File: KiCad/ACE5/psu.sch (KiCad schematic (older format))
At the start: 29 parts, among them IC1 LM7805MPX_NOPB

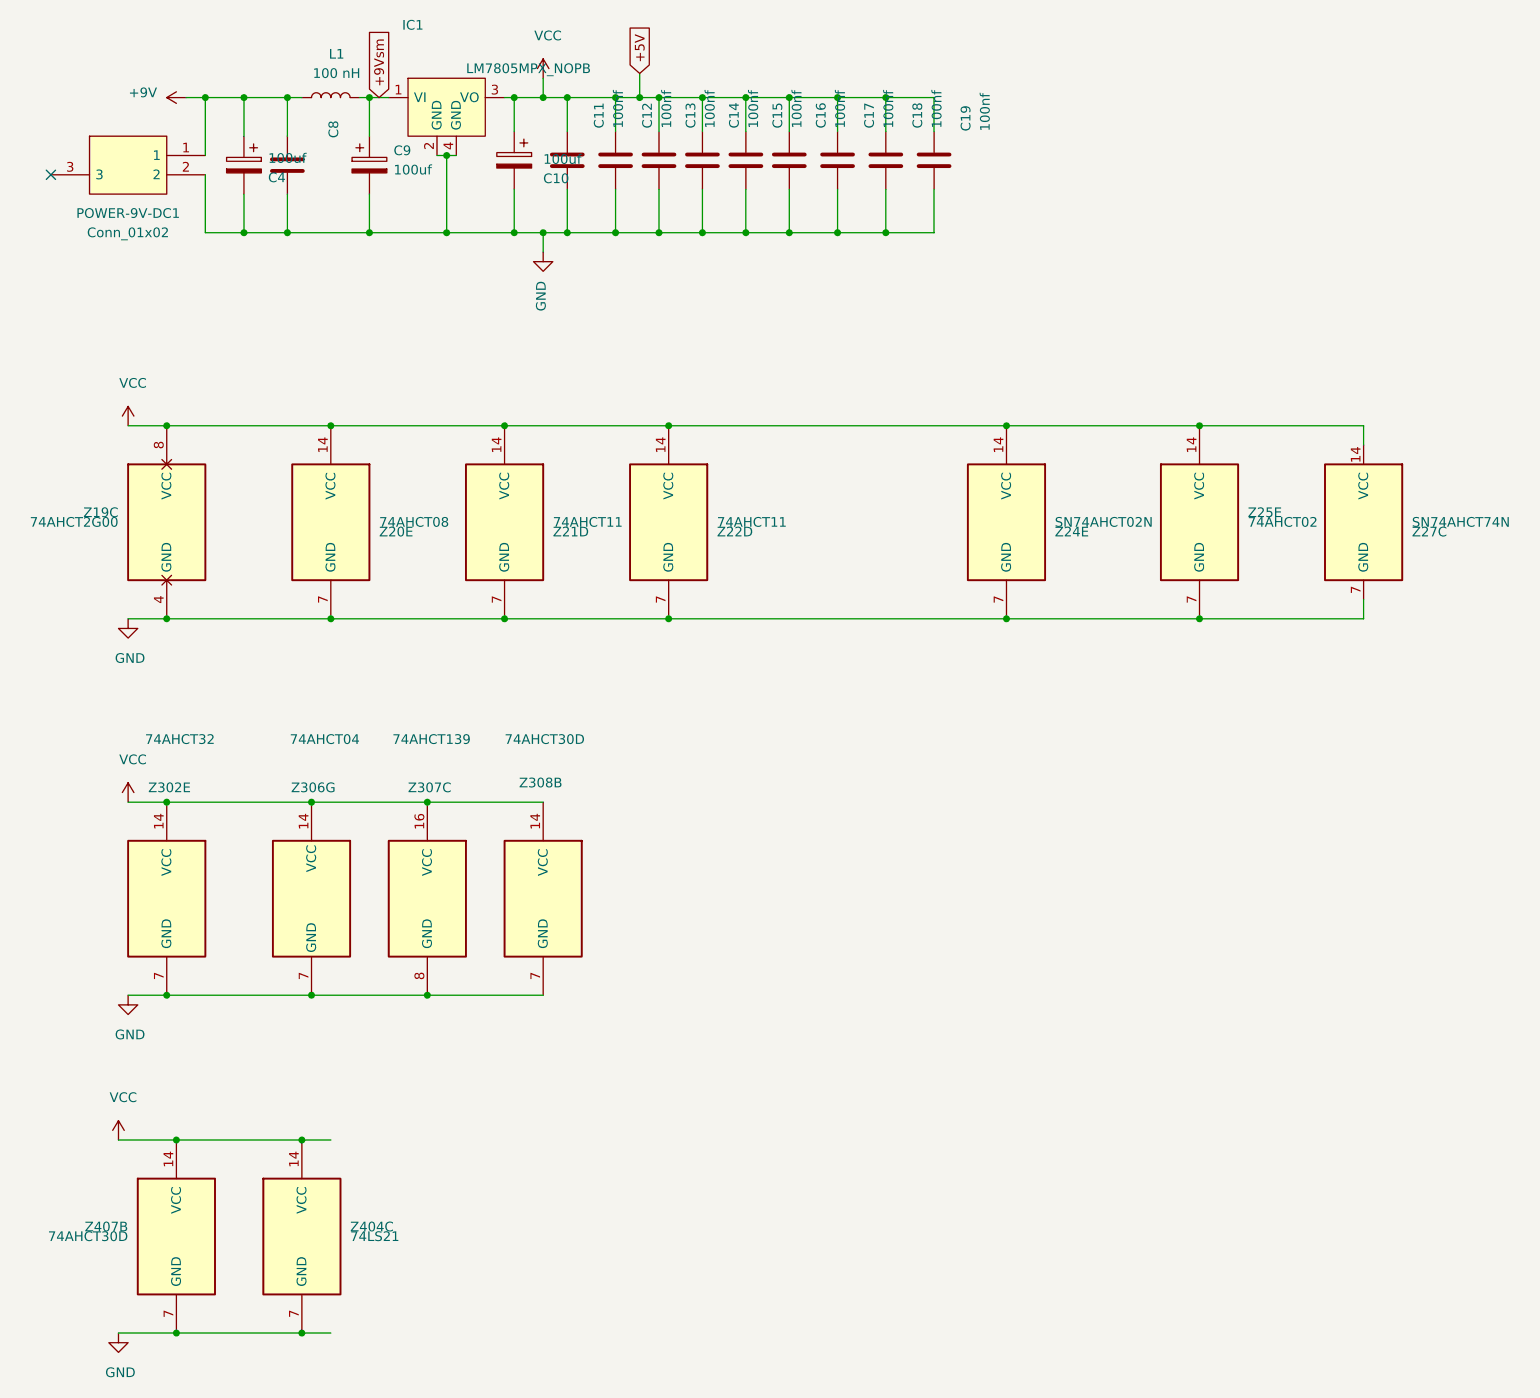
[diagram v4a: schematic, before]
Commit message: Fix several problems with Chip Select. Reconnect the Data bus for the VDG to the CPU bus which has become disconnected.
Signed-off-by: John Bradley <flypie@rocketmail.com>
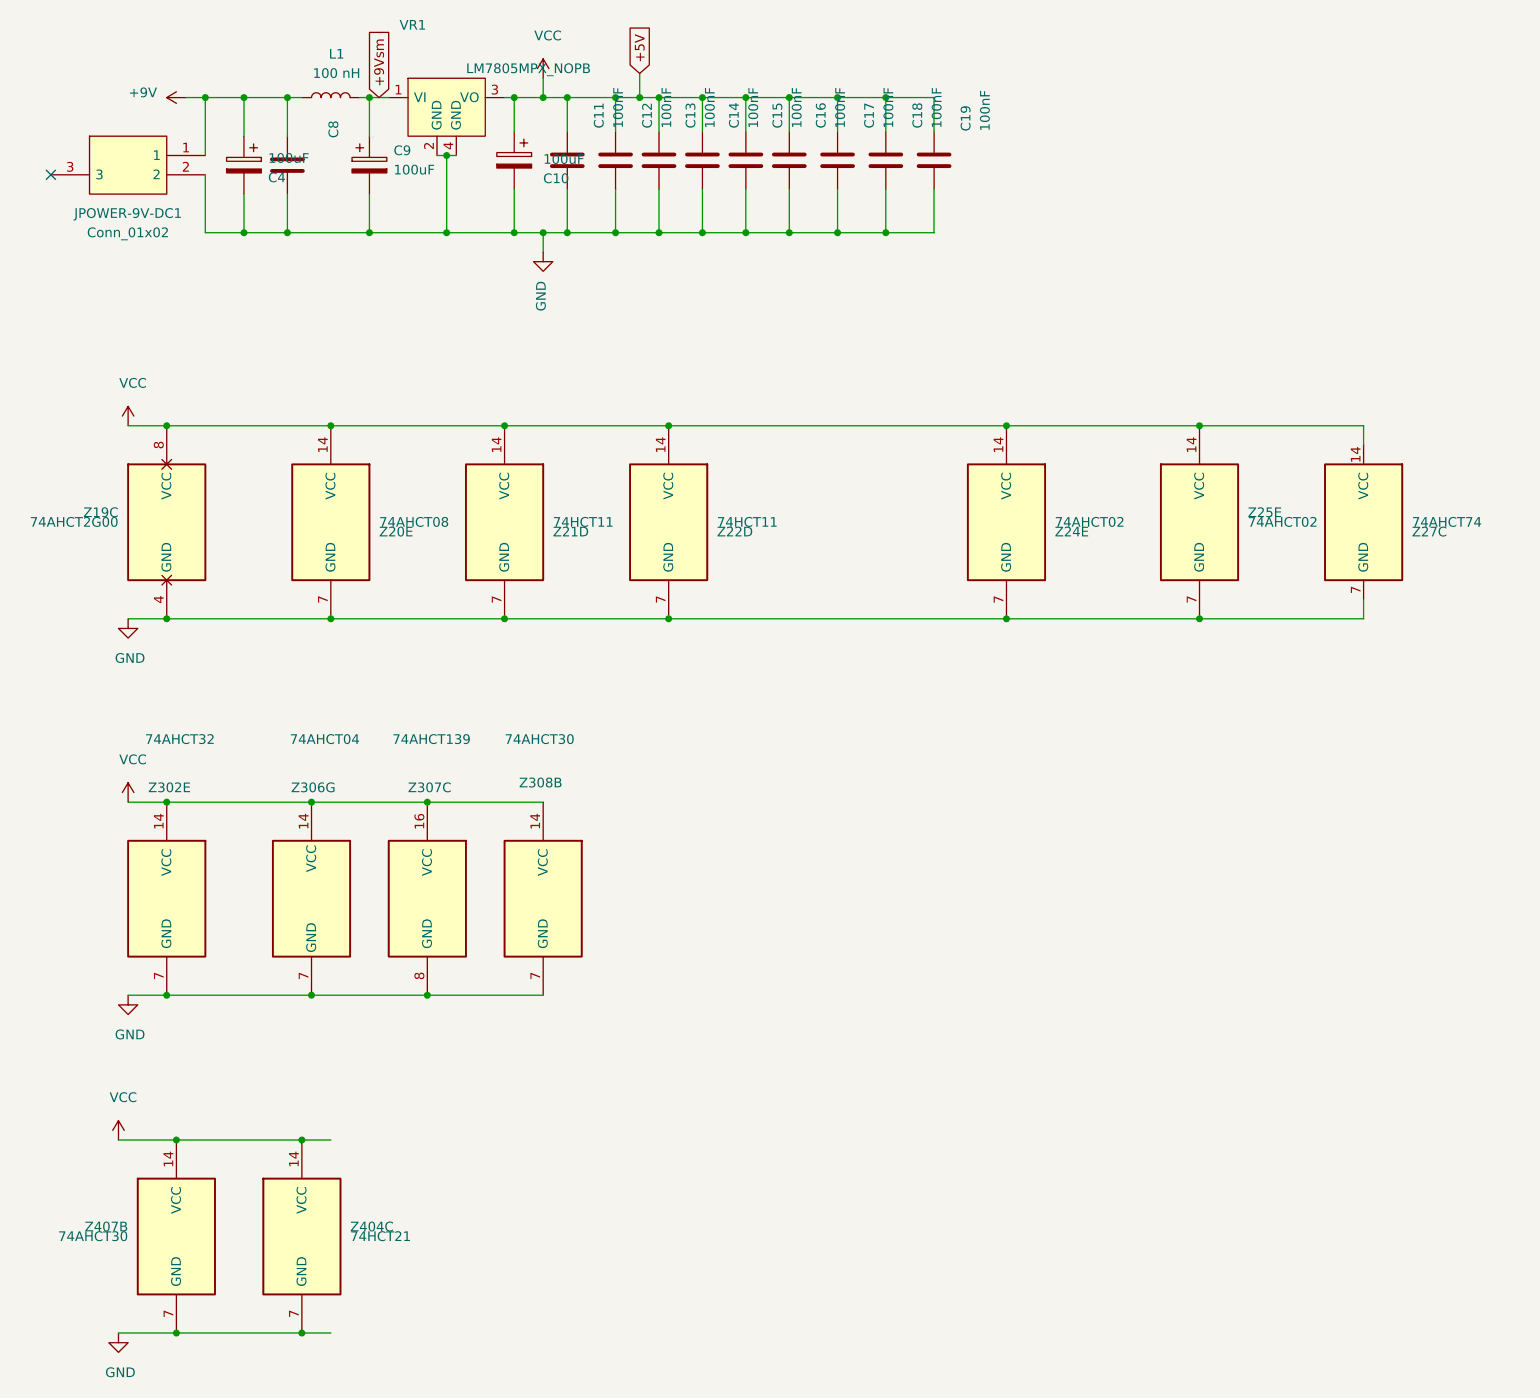
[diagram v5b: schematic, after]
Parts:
- C10, C4: value 100uf -> 100uF; footprint Capacitor_SMD:CP_Elec_6.3x5.3 -> Capacitor_SMD:CP_Elec_5x5.7; Manufacturer_Name (none) -> Wurth Elektronik; Manufacturer_Part_Number (none) -> 865080142007
- C11, C12, C13, C14, C15, C16, C17, C18, C19, C8: value 100nf -> 100nF; Manufacturer_Name Vishay -> Samsung Electro-Mechanics; Manufacturer_Part_Number K104K10X7RF53H5 -> CL31B104KBCNNNC
- C9: value 100uf -> 100uF; footprint Capacitor_SMD:CP_Elec_6.3x5.3 -> Capacitor_SMD:CP_Elec_5x5.7; Manufacturer_Name Vishay -> Wurth Elektronik; Manufacturer_Part_Number K104K10X7RF53H5 -> 865080142007
- JPOWER-9V-DC1: renamed from POWER-9V-DC1; Manufacturer_Name (none) -> CUI Devices; Manufacturer_Part_Number (none) -> PJ-036AH-SMT-TR
- L1: Manufacturer_Name (none) -> Bussmann / Eaton; Manufacturer_Part_Number (none) -> MCQ1V3216-R100-R
- Z19: footprint Package_SO:TSSOP-8_3x3mm_P0.65mm -> Package_SO:VSSOP-8_2.4x2.1mm_P0.5mm; Manufacturer_Part_Number SN74AHCT00N -> 74AHCT2G00DC,125
- Z20: Manufacturer_Name (none) -> Texas Instruments; Manufacturer_Part_Number (none) -> SN74AHCT08DR
- Z21, Z22: value 74AHCT11 -> 74HCT11; footprint Package_SO:SOIC-14_3.9x8.7mm_P1.27mm -> Package_SO:SO-14_3.9x8.65mm_P1.27mm; Manufacturer_Name (none) -> Nexperia; Manufacturer_Part_Number (none) -> 74HCT11D,653
- Z24: value SN74AHCT02N -> 74AHCT02; Manufacturer_Name (none) -> Texas Instruments; Manufacturer_Part_Number (none) -> SN74AHCT02DR
- Z25: Manufacturer_Part_Number SN74AHCT00N -> SN74AHCT02DR
- Z27: value SN74AHCT74N -> 74AHCT74; Manufacturer_Name (none) -> Texas Instruments; Manufacturer_Part_Number (none) -> SN74AHCT74DR
- Z302: Manufacturer_Name (none) -> Texas Instruments; Manufacturer_Part_Number (none) -> SN74AHCT32DR
- Z306: footprint Package_SO:SOIC-16_3.9x9.9mm_P1.27mm -> Package_SO:SOIC-14_3.9x8.7mm_P1.27mm; Manufacturer_Name (none) -> Texas Instruments; Manufacturer_Part_Number (none) -> SN74AHCT04DR
- Z307: Manufacturer_Name (none) -> Nexperia; Manufacturer_Part_Number (none) -> 74AHCT139D,118
- Z308: value 74AHCT30D -> 74AHCT30; footprint Package_SO:SOIC-14_3.9x8.7mm_P1.27mm -> Package_SO:SO-14_3.9x8.65mm_P1.27mm; Manufacturer_Name NEXPERIA -> Nexperia; Manufacturer_Part_Number 74AHCT30D -> 74AHCT30D-Q100J
- Z404: value 74LS21 -> 74HCT21; Manufacturer_Name (none) -> Texas Instruments; Manufacturer_Part_Number (none) -> CD74HCT21M96
- Z407: value 74AHCT30D -> 74AHCT30; footprint Package_SO:SOIC-14_3.9x8.7mm_P1.27mm -> Package_SO:SO-14_3.9x8.65mm_P1.27mm; Manufacturer_Name (none) -> Nexperia; Manufacturer_Part_Number (none) -> 74AHCT30D-Q100J
- renumbered IC1 to VR1
